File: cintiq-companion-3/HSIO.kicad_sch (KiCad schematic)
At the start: 25 parts, among them J3 Bus_M.2_Socket_M, J4 Bus_M.2_Socket_E, J5 Bus_M.2_Socket_B, J6 USB3_A

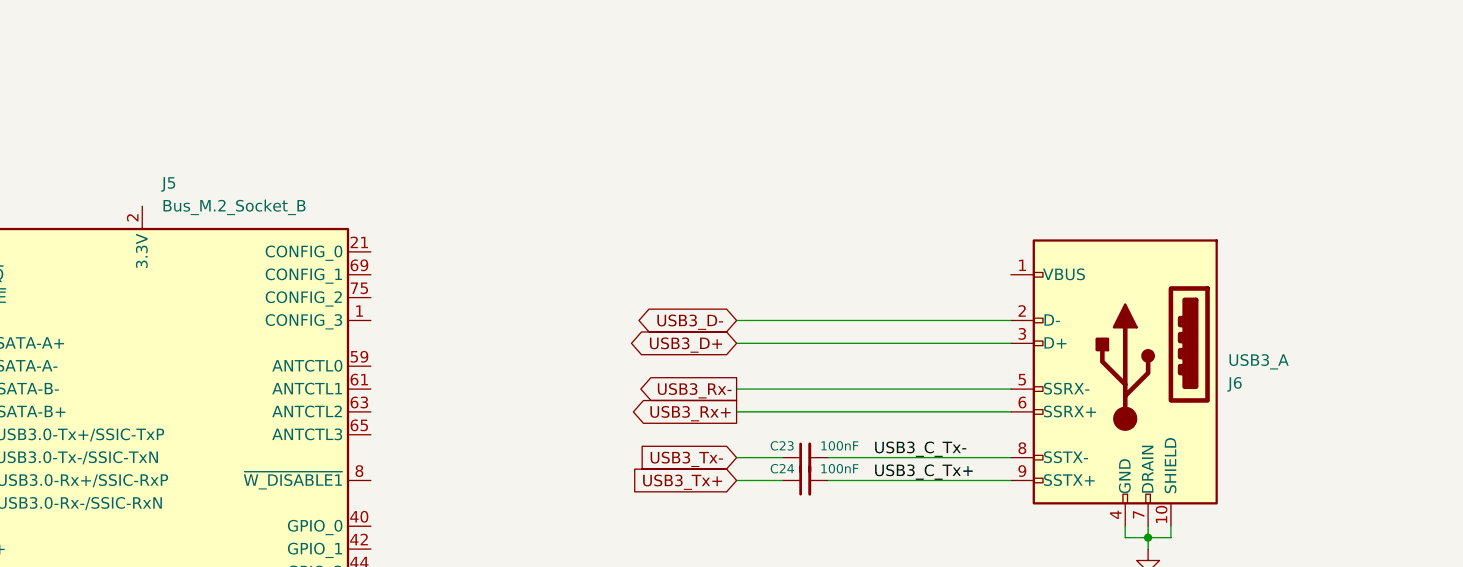
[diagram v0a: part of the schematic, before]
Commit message: Started adding type-c
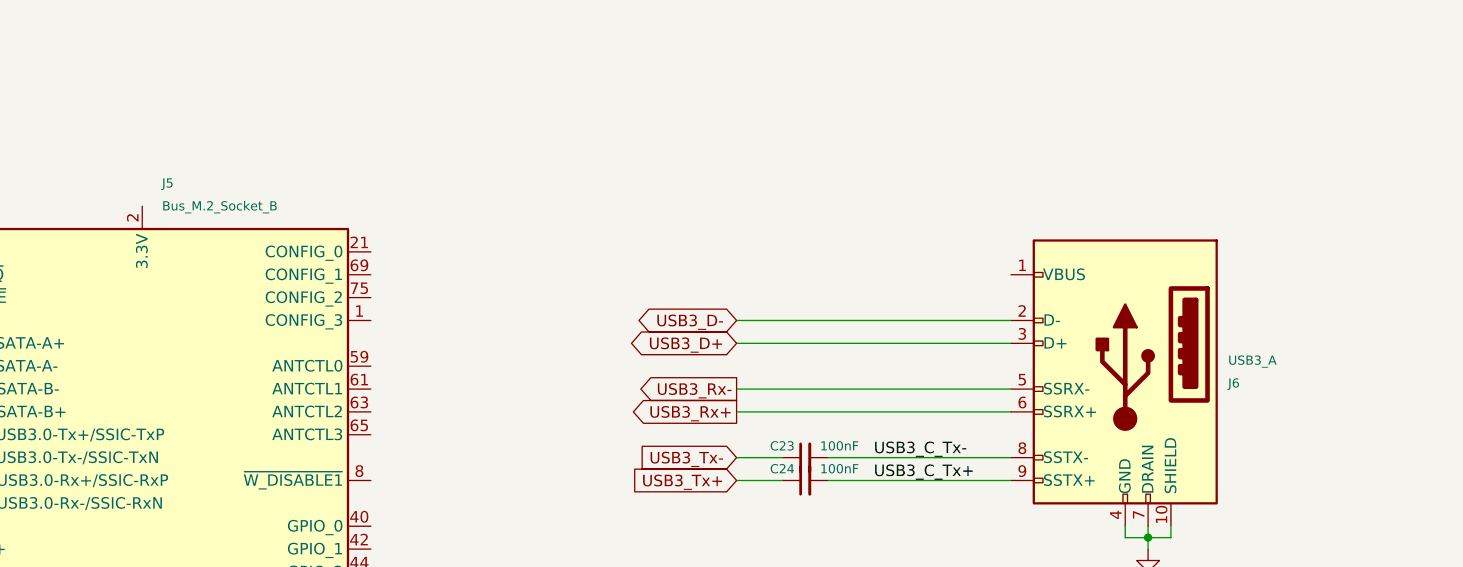
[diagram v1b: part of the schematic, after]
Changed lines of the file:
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@@
 			(effects
 				(font
-					(size 1.27 1.27)
+					(size 1.016 1.016)
 				)
 				(justify left)
@@
 			(effects
 				(font
-					(size 1.27 1.27)
+					(size 1.016 1.016)
 				)
 				(justify left)
@@
 			(effects
 				(font
-					(size 1.27 1.27)
+					(size 1.016 1.016)
 				)
 				(justify right)
@@
 			(effects
 				(font
-					(size 1.27 1.27)
+					(size 1.016 1.016)
 				)
 				(justify right)

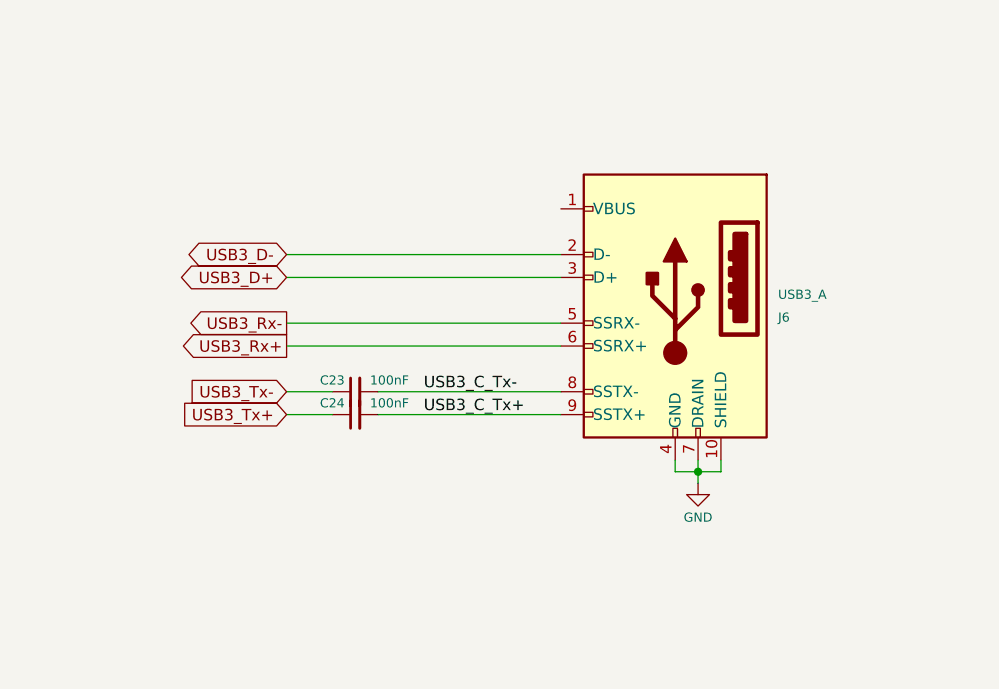
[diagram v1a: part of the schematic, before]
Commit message: flipped b-key lane order and added usb-c ports
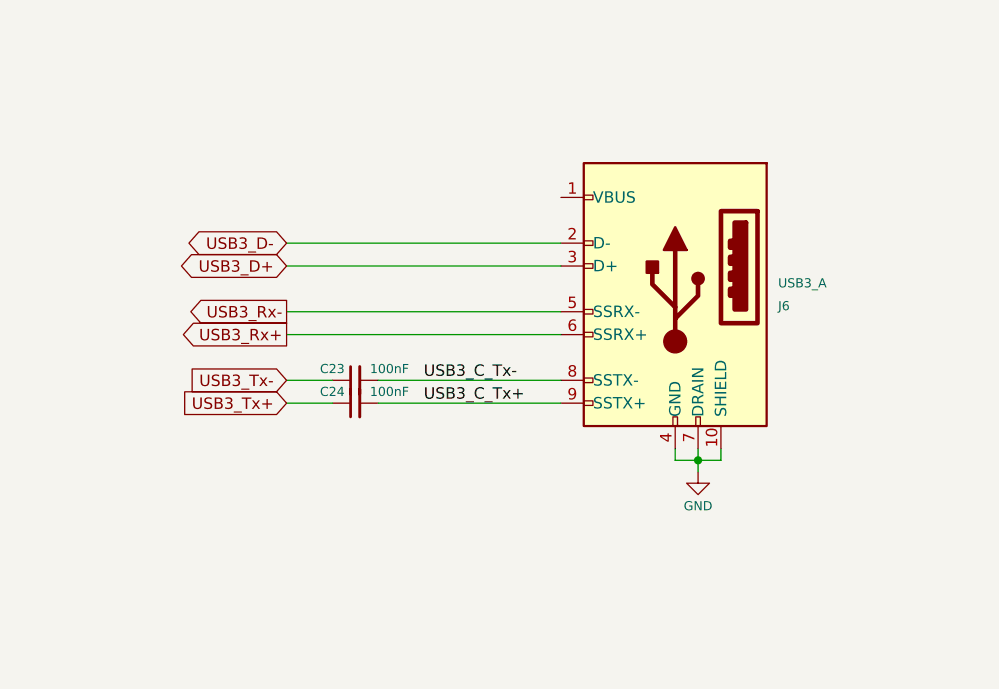
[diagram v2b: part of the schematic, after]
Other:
- moved on the sheet: C23, C24, J6
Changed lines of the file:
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@@
 	)
 	(junction
-		(at 220.98 207.01)
+		(at 220.98 205.74)
 		(diameter 0)
 		(color 0 0 0 0)
@@
 	(wire
 		(pts
-			(xy 175.26 198.12) (xy 180.34 198.12)
+			(xy 175.26 196.85) (xy 180.34 196.85)
 		)
 		(stroke
@@
 	(wire
 		(pts
-			(xy 218.44 205.74) (xy 218.44 207.01)
+			(xy 218.44 204.47) (xy 218.44 205.74)
 		)
 		(stroke
@@
 	(wire
 		(pts
-			(xy 218.44 207.01) (xy 220.98 207.01)
+			(xy 218.44 205.74) (xy 220.98 205.74)
 		)
 		(stroke
@@
 	(wire
 		(pts
-			(xy 185.42 200.66) (xy 205.74 200.66)
+			(xy 185.42 199.39) (xy 205.74 199.39)
 		)
 		(stroke
@@
 	(wire
 		(pts
-			(xy 223.52 205.74) (xy 223.52 207.01)
+			(xy 223.52 204.47) (xy 223.52 205.74)
 		)
 		(stroke
@@
 	(wire
 		(pts
-			(xy 175.26 182.88) (xy 205.74 182.88)
+			(xy 175.26 181.61) (xy 205.74 181.61)
 		)
 		(stroke
@@
 	(wire
 		(pts
-			(xy 220.98 207.01) (xy 220.98 208.28)
+			(xy 220.98 205.74) (xy 220.98 207.01)
 		)
 		(stroke
@@
 	(wire
 		(pts
-			(xy 220.98 207.01) (xy 223.52 207.01)
+			(xy 220.98 205.74) (xy 223.52 205.74)
 		)
 		(stroke
@@
 	(wire
 		(pts
-			(xy 175.26 200.66) (xy 180.34 200.66)
+			(xy 175.26 199.39) (xy 180.34 199.39)
 		)
 		(stroke
@@
 	(wire
 		(pts
-			(xy 220.98 205.74) (xy 220.98 207.01)
+			(xy 220.98 204.47) (xy 220.98 205.74)
 		)
 		(stroke
@@
 	(wire
 		(pts
-			(xy 175.26 193.04) (xy 205.74 193.04)
+			(xy 175.26 191.77) (xy 205.74 191.77)
 		)
 		(stroke
@@
 	(wire
 		(pts
-			(xy 175.26 190.5) (xy 205.74 190.5)
+			(xy 175.26 189.23) (xy 205.74 189.23)
 		)
 		(stroke
@@
 	(wire
 		(pts
-			(xy 185.42 198.12) (xy 205.74 198.12)
+			(xy 185.42 196.85) (xy 205.74 196.85)
 		)
 		(stroke
@@
 	(wire
 		(pts
-			(xy 175.26 185.42) (xy 205.74 185.42)
+			(xy 175.26 184.15) (xy 205.74 184.15)
 		)
 		(stroke
@@
 	)
 	(label "USB3_C_Tx+"
-		(at 190.5 200.66 0)
+		(at 190.5 199.39 0)
 		(fields_autoplaced yes)
 		(effects
@@
 	)
 	(label "USB3_C_Tx-"
-		(at 190.5 198.12 0)
+		(at 190.5 196.85 0)
 		(fields_autoplaced yes)
 		(effects
@@
 	(global_label "USB3_Tx-"
 		(shape input)
-		(at 175.26 198.12 180)
+		(at 175.26 196.85 180)
 		(fields_autoplaced yes)
 		(effects
@@
 		)
 		(property "Intersheetrefs" "${INTERSHEET_REFS}"
-			(at 162.7196 198.12 0)
+			(at 162.7196 196.85 0)
 			(effects
 				(font
@@
 	(global_label "USB3_Rx-"
 		(shape output)
-		(at 175.26 190.5 180)
+		(at 175.26 189.23 180)
 		(fields_autoplaced yes)
 		(effects
@@
 		)
 		(property "Intersheetrefs" "${INTERSHEET_REFS}"
-			(at 162.4172 190.5 0)
+			(at 162.4172 189.23 0)
 			(effects
 				(font
@@
 	(global_label "USB3_Rx+"
 		(shape output)
-		(at 175.26 193.04 180)
+		(at 175.26 191.77 180)
 		(fields_autoplaced yes)
 		(effects
@@
 		)
 		(property "Intersheetrefs" "${INTERSHEET_REFS}"
-			(at 162.4172 193.04 0)
+			(at 162.4172 191.77 0)
 			(effects
 				(font
@@
 	(global_label "USB3_D-"
 		(shape bidirectional)
-		(at 175.26 182.88 180)
+		(at 175.26 181.61 180)
 		(fields_autoplaced yes)
 		(effects
@@
 		)
 		(property "Intersheetrefs" "${INTERSHEET_REFS}"
-			(at 162.334 182.88 0)
+			(at 162.334 181.61 0)
 			(effects
 				(font
@@
 	(global_label "USB3_D+"
 		(shape bidirectional)
-		(at 175.26 185.42 180)
+		(at 175.26 184.15 180)
 		(fields_autoplaced yes)
 		(effects
@@
 		)
 		(property "Intersheetrefs" "${INTERSHEET_REFS}"
-			(at 162.334 185.42 0)
+			(at 162.334 184.15 0)
 			(effects
 				(font
@@
 	(global_label "USB3_Tx+"
 		(shape input)
-		(at 175.26 200.66 180)
+		(at 175.26 199.39 180)
 		(fields_autoplaced yes)
 		(effects
@@
 		)
 		(property "Intersheetrefs" "${INTERSHEET_REFS}"
-			(at 162.7196 200.66 0)
+			(at 162.7196 199.39 0)
 			(effects
 				(font
@@
 	(symbol
 		(lib_id "Device:C_Small")
-		(at 182.88 200.66 90)
+		(at 182.88 199.39 90)
 		(unit 1)
 		(exclude_from_sim no)
@@
 		(dnp no)
 		(property "Reference" "C24"
-			(at 180.34 199.39 90)
+			(at 180.34 198.12 90)
 			(effects
 				(font
@@
 		)
 		(property "Value" "100nF"
-			(at 186.69 199.39 90)
+			(at 186.69 198.12 90)
 			(effects
 				(font
@@
 		)
 		(property "Footprint" "Capacitor_SMD:C_0402_1005Metric"
-			(at 182.88 200.66 0)
+			(at 182.88 199.39 0)
 			(effects
 				(font
@@
 		)
 		(property "Datasheet" "~"
-			(at 182.88 200.66 0)
+			(at 182.88 199.39 0)
 			(effects
 				(font
@@
 		)
 		(property "Description" "Unpolarized capacitor, small symbol"
-			(at 182.88 200.66 0)
+			(at 182.88 199.39 0)
 			(effects
 				(font
@@
 	(symbol
 		(lib_id "power:GND")
-		(at 220.98 208.28 0)
+		(at 220.98 207.01 0)
 		(unit 1)
 		(exclude_from_sim no)
@@
 		(dnp no)
 		(property "Reference" "#PWR024"
-			(at 220.98 214.63 0)
+			(at 220.98 213.36 0)
 			(effects
 				(font
@@
 		)
 		(property "Value" "GND"
-			(at 220.98 212.09 0)
+			(at 220.98 210.82 0)
 			(effects
 				(font
@@
 		)
 		(property "Footprint" ""
-			(at 220.98 208.28 0)
+			(at 220.98 207.01 0)
 			(effects
 				(font
@@
 		)
 		(property "Datasheet" ""
-			(at 220.98 208.28 0)
+			(at 220.98 207.01 0)
 			(effects
 				(font
@@
 		)
 		(property "Description" ""
-			(at 220.98 208.28 0)
+			(at 220.98 207.01 0)
 			(effects
 				(font
@@
 	(symbol
 		(lib_id "Device:C_Small")
-		(at 182.88 198.12 90)
+		(at 182.88 196.85 90)
 		(unit 1)
 		(exclude_from_sim no)
@@
 		(dnp no)
 		(property "Reference" "C23"
-			(at 180.34 196.85 90)
+			(at 180.34 195.58 90)
 			(effects
 				(font
@@
 		)
 		(property "Value" "100nF"
-			(at 186.69 196.85 90)
+			(at 186.69 195.58 90)
 			(effects
 				(font
@@
 		)
 		(property "Footprint" "Capacitor_SMD:C_0402_1005Metric"
-			(at 182.88 198.12 0)
+			(at 182.88 196.85 0)
 			(effects
 				(font
@@
 		)
 		(property "Datasheet" "~"
-			(at 182.88 198.12 0)
+			(at 182.88 196.85 0)
 			(effects
 				(font
@@
 		)
 		(property "Description" "Unpolarized capacitor, small symbol"
-			(at 182.88 198.12 0)
+			(at 182.88 196.85 0)
 			(effects
 				(font
@@
 	(symbol
 		(lib_id "Connector:USB3_A")
-		(at 218.44 187.96 0)
+		(at 218.44 186.69 0)
 		(mirror y)
 		(unit 1)
@@
 		(dnp no)
 		(property "Reference" "J6"
-			(at 229.87 189.8651 0)
+			(at 229.87 188.5951 0)
 			(effects
 				(font
@@
 		)
 		(property "Value" "USB3_A"
-			(at 229.87 187.3251 0)
+			(at 229.87 186.0551 0)
 			(effects
 				(font
@@
 		)
 		(property "Footprint" ""
-			(at 214.63 185.42 0)
+			(at 214.63 184.15 0)
 			(effects
 				(font
@@
 		)
 		(property "Datasheet" "~"
-			(at 214.63 185.42 0)
+			(at 214.63 184.15 0)
 			(effects
 				(font
@@
 		)
 		(property "Description" "USB 3.0 A connector"
-			(at 218.44 187.96 0)
+			(at 218.44 186.69 0)
 			(effects
 				(font

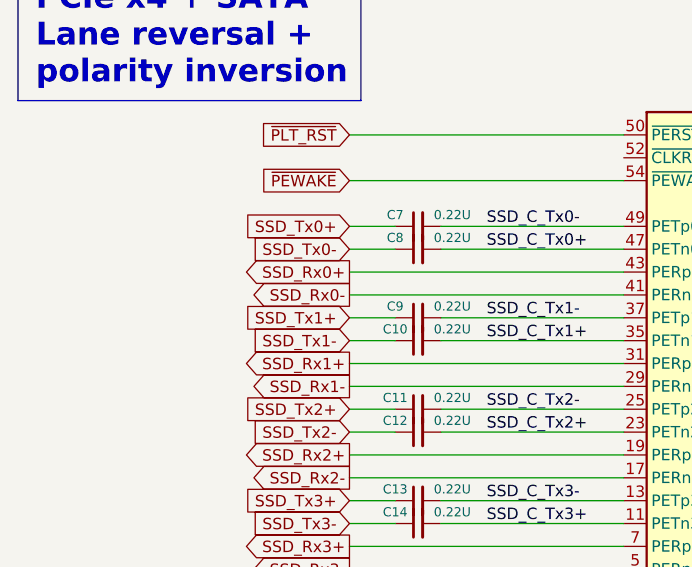
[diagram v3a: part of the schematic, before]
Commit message: Swapped sata pair polarity on m-key slot to make sata actually work probably
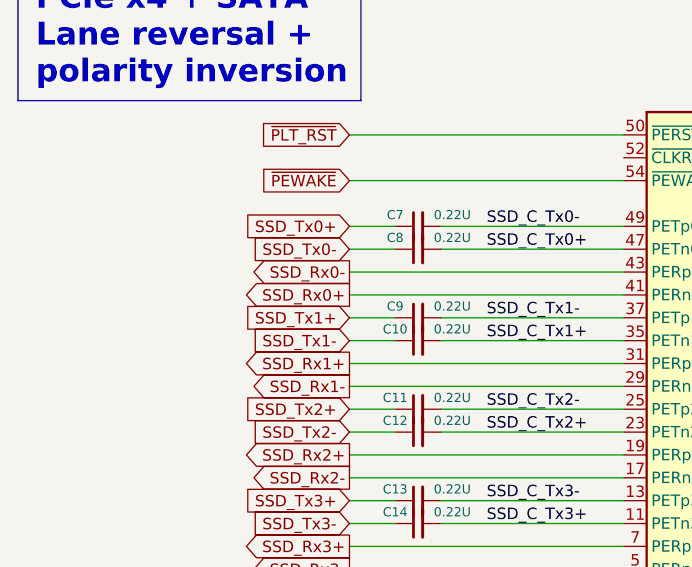
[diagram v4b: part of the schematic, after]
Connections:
- net SSD_Rx0+: now also J3.41 (PERn0/SATA-B+); no longer J3.43 (PERp0/SATA-B-)
- net SSD_Rx0-: now also J3.43 (PERp0/SATA-B-); no longer J3.41 (PERn0/SATA-B+)
